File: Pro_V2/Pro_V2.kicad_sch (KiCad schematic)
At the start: 322 parts, among them J1 USB_C_Receptacle, J2 AudioJack4, J3 OLED, J6 USB_C_Receptacle, J7 OLED, J8 AudioJack4, SW1 SW_Push, SW10 SW_Push, SW11 SW_Push, SW12 SW_Push, SW13 SW_Push, SW14 SW_Push, SW15 SW_Push, SW16 SW_Push, SW17 SW_Push, SW18 SW_Push, SW19 SW_Push, SW2 SW_Push, SW20 SW_Push, SW21 SW_Push, SW22 SW_Push, SW23 SW_Push, SW24 SW_Push, SW25 SW_Push, SW26 SW_Push, SW27 SW_Push, SW28 SW_Push, SW29 SW_Push, SW3 SW_Push, SW30 SW_Push, SW31 SW_Push, SW32 SW_Push, SW33 SW_Push, SW34 SW_Push, SW35 SW_Push, SW36 SW_Push, SW37 SW_Push, SW38 SW_Push, SW39 SW_Push, SW4 SW_Push, SW40 SW_Push, SW41 SW_Push, SW42 SW_Push, SW43 SW_Push, SW44 SW_Push, SW45 SW_Push, SW46 SW_Push, SW47 SW_Push, SW48 SW_Push, SW49 SW_Push, SW5 SW_Push, SW50 SW_Push, SW51 SW_Push, SW52 SW_Push, SW53 SW_Push, SW54 SW_Push, SW55 SW_Push, SW56 SW_Push, SW57 SW_Push, SW58 SW_Push, SW6 SW_Push, SW7 SW_Push, SW8 SW_Push, SW9 SW_Push, U1 AMS1117-3.3, U10 TXB0104RUT, U2 USBLC6-2SC6, U3 RP2040, U4 W25Q128JVPIQ, U5 AMS1117-3.3, U6 USBLC6-2SC6, U7 RP2040, U8 W25Q128JVPIQ, U9 TXB0104RUT, Y1 12MHz, Y2 12MHz

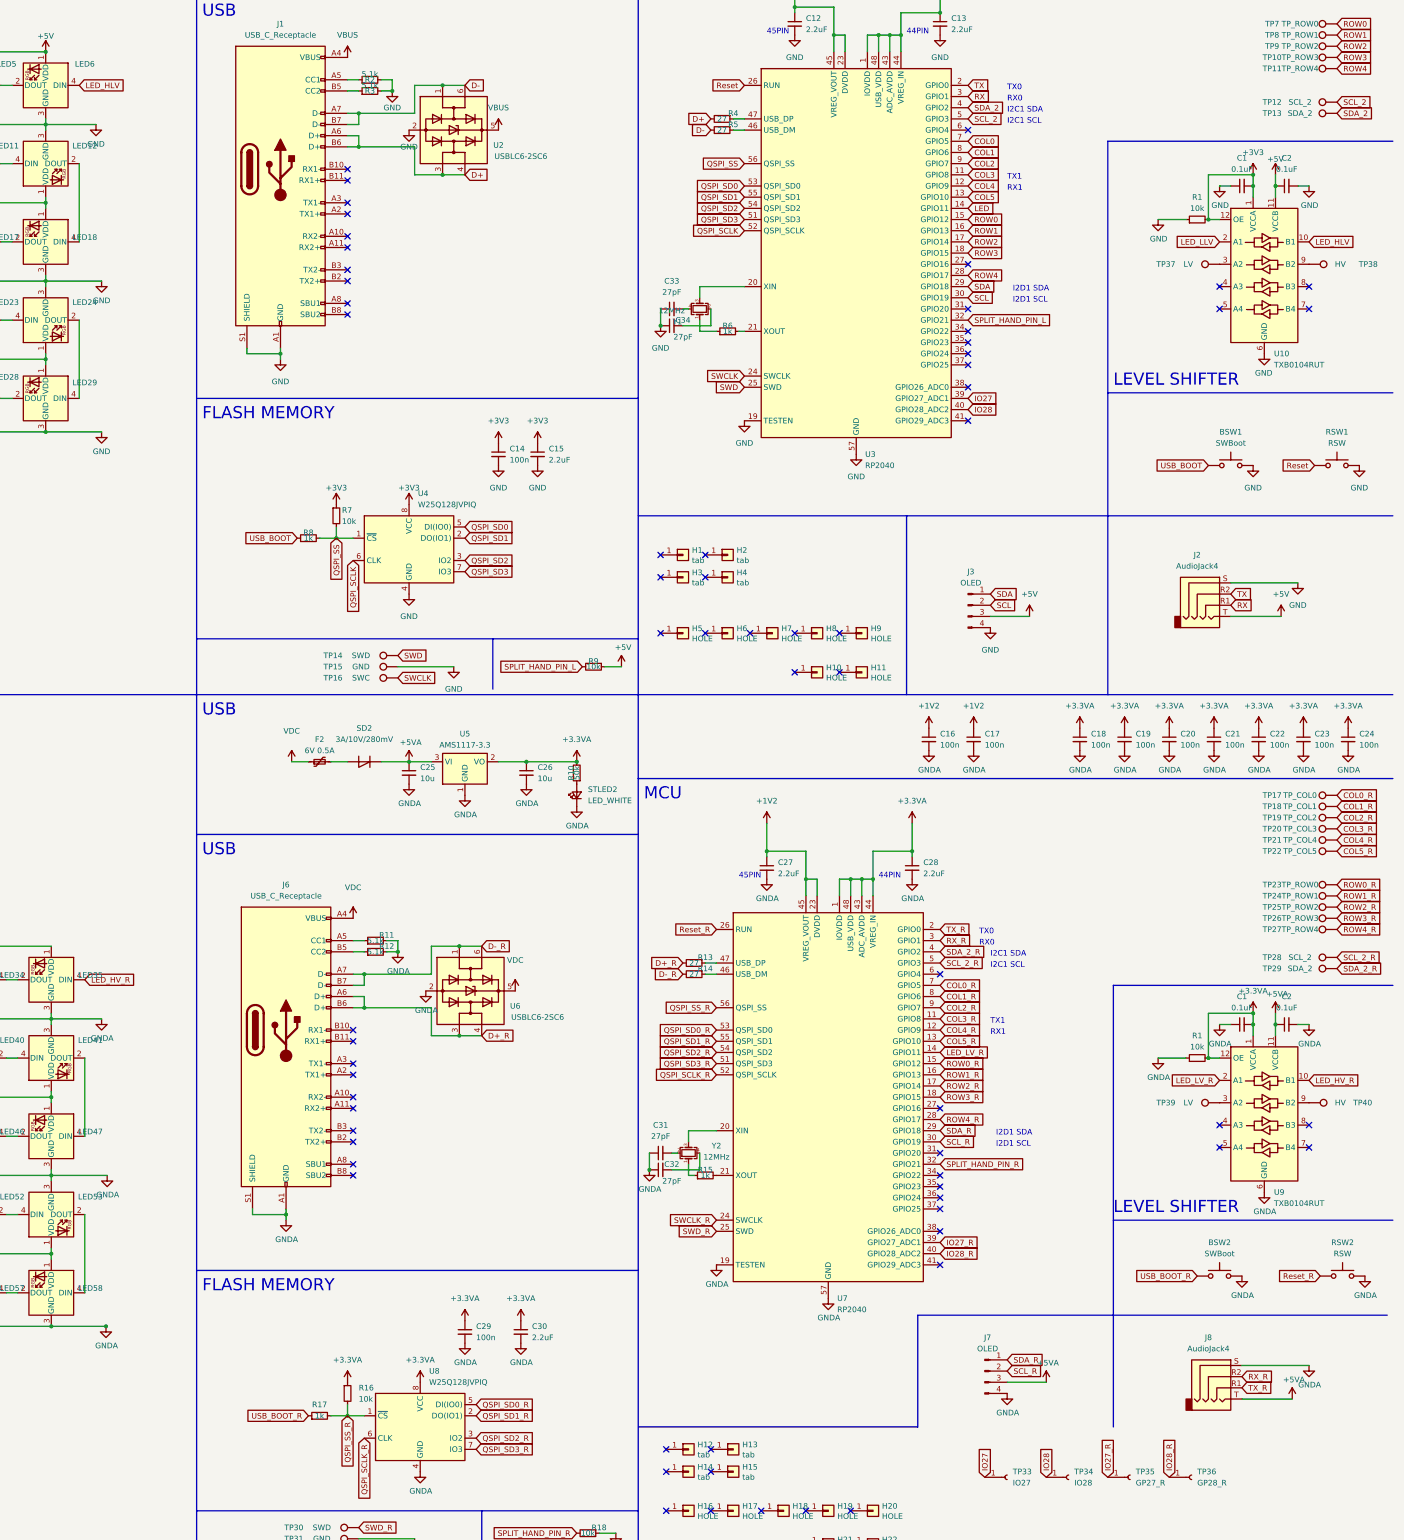
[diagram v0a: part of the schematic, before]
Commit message: [Lily58 Lite Rev3] Fix SW54
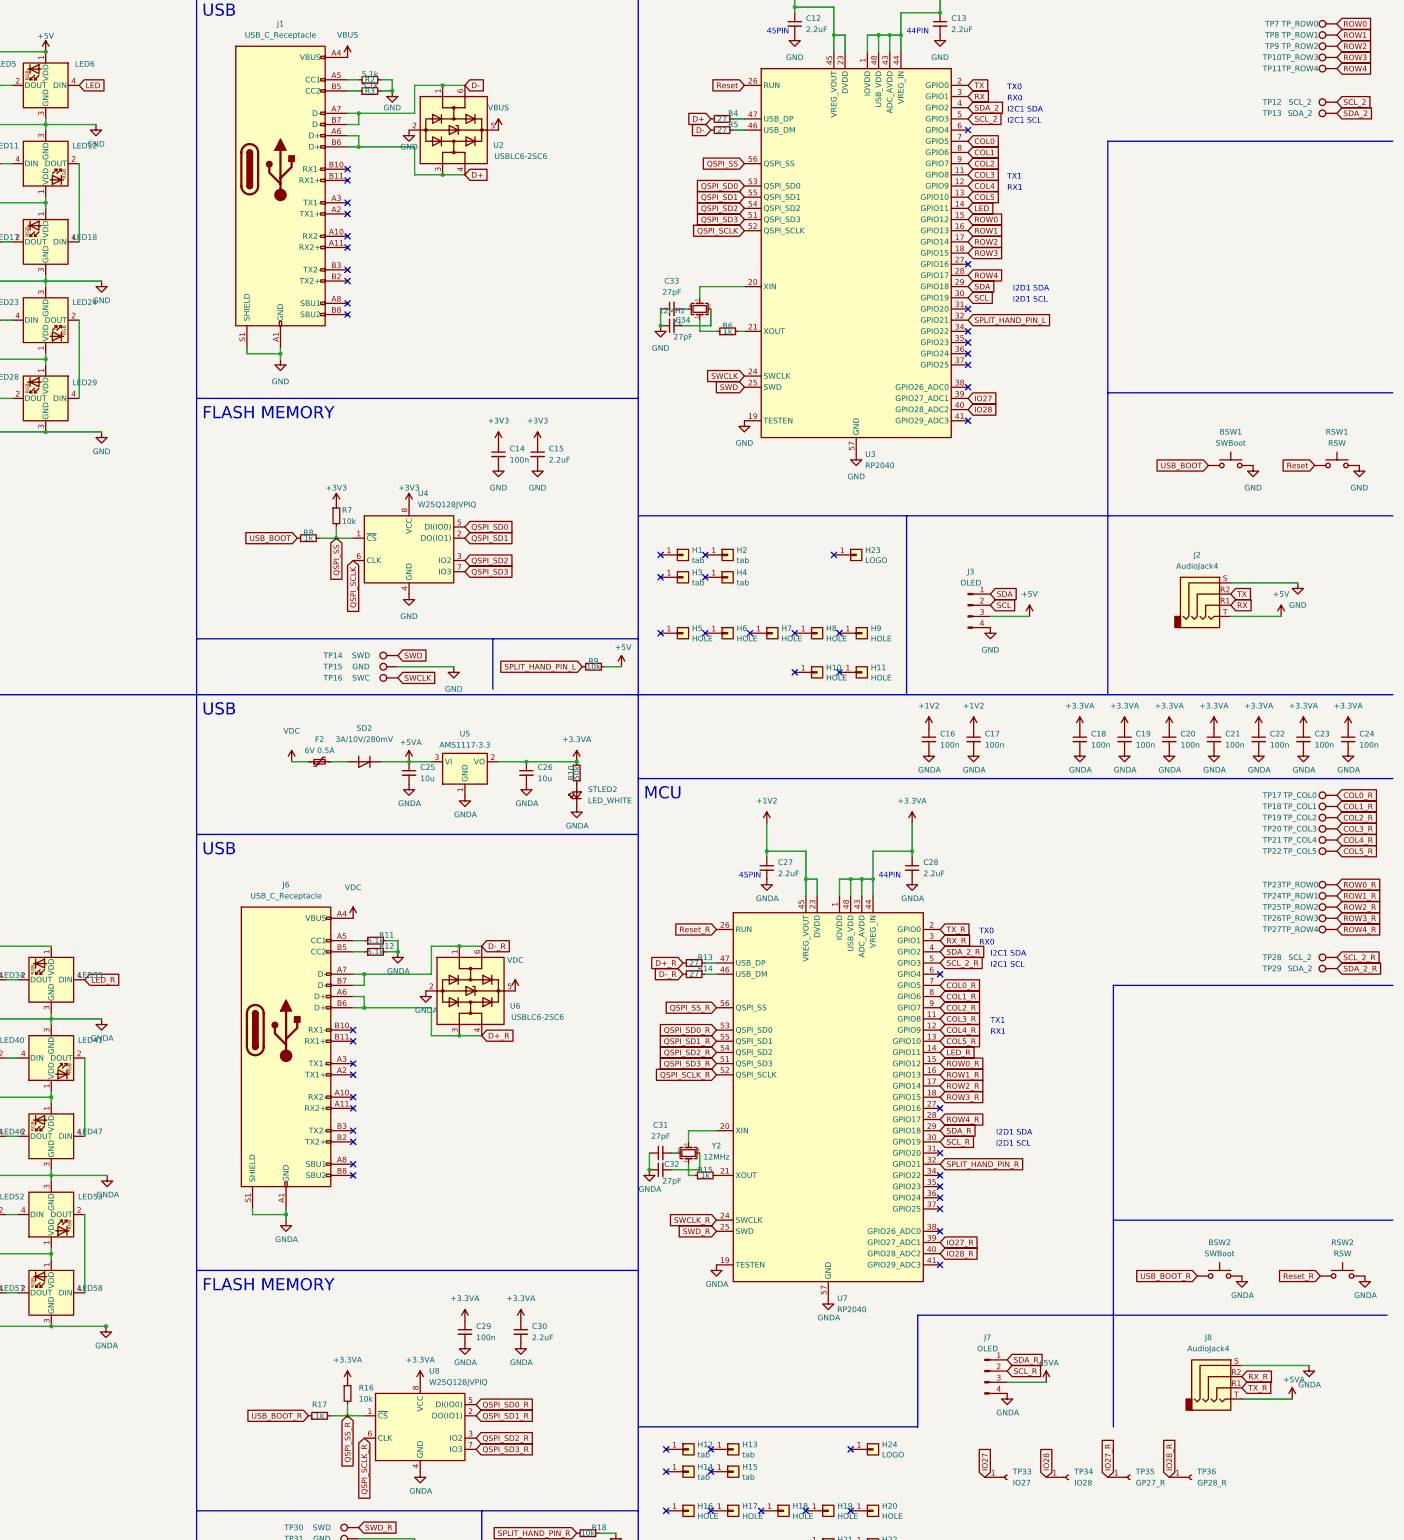
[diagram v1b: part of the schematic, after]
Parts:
- removed C1 (x2), C2 (x2): 0.1uF, Capacitor_SMD:C_0402_1005Metric, symbol Device:C_Small
- removed R1 (x2): 10k, Resistor_SMD:R_0402_1005Metric, symbol Device:R_Small
- removed TP37, TP39: LV, yuchi:TestPoint_Pad_1mm, symbol Connector:TestPoint
- removed TP38, TP40: HV, yuchi:TestPoint_Pad_1mm, symbol Connector:TestPoint
- removed U10, U9: TXB0104RUT, Package_DFN_QFN:Texas_R-PUQFN-N12, symbol Logic_LevelTranslator:TXB0104RUT
- added H23, H24: LOGO, yuchi:lily58_logo_2, symbol Connector_Generic:Conn_01x01
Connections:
- net LED_HLV is gone; now on net LED: LED6.4 (DIN)
- net LED_LV_R is gone; now on net LED_R: U7.14 (GPIO11)
- net LED_HV_R renamed LED_R
- no-connect marks 70 -> 64
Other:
- note removed: "LEVEL SHIFTER"

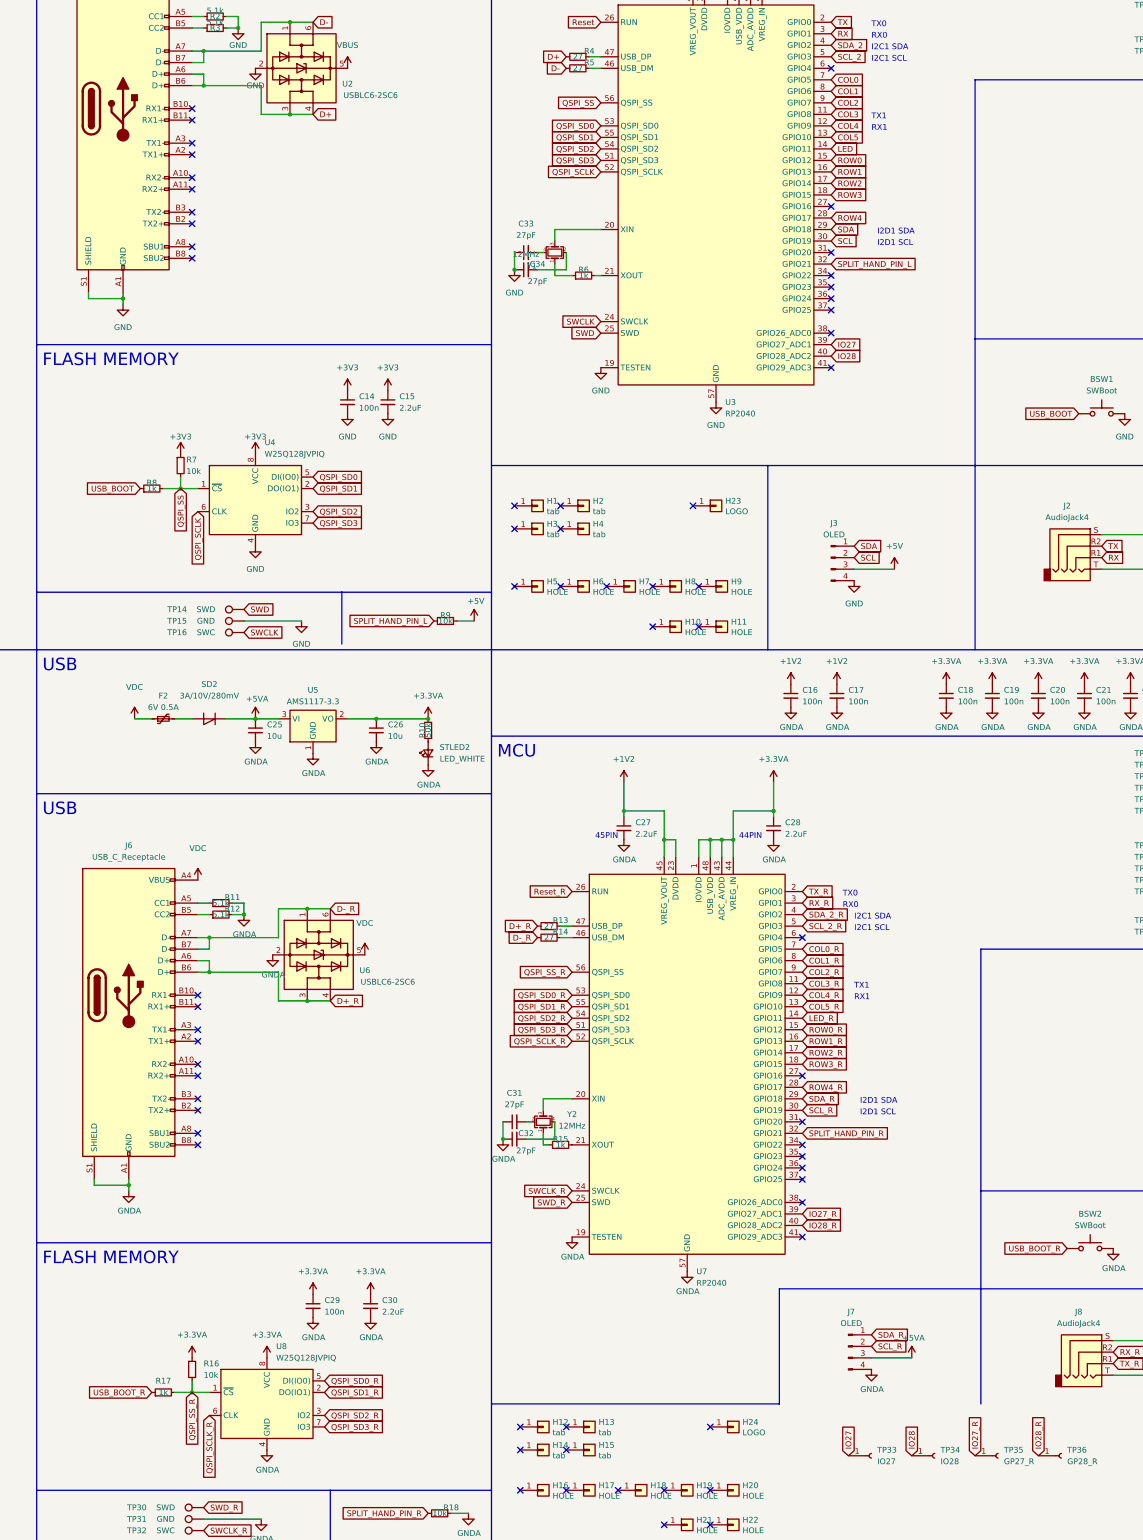
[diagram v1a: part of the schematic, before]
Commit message: fix SPLIT_HAND_PIN_L Pin #57
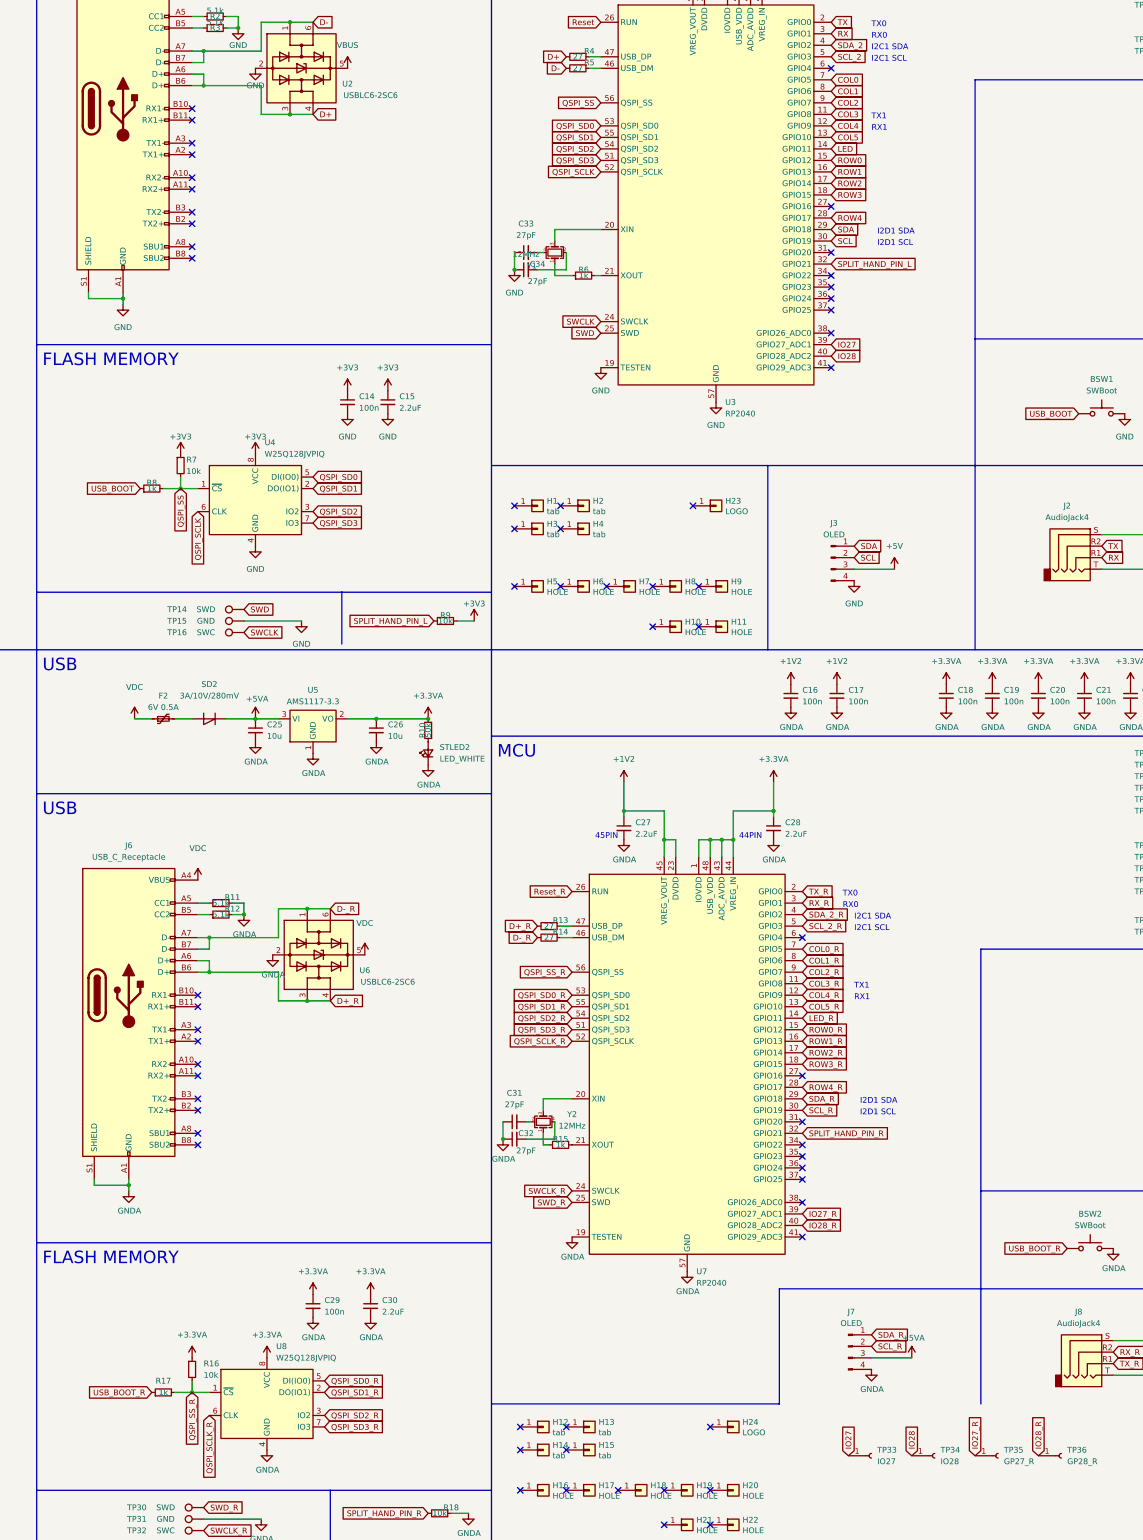
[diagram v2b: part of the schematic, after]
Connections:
- net +3V3: now also R9.1
- net +5V: no longer R9.1
